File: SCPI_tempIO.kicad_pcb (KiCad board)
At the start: 2 copper layers, 40.4 x 21.5 mm, 27 parts, among them J1 Conn_ARM_JTAG_SWD_10, J2 Conn_02x05_Counter_Clockwise, J3 USB_C_Receptacle_USB2.0_14P, J4 Conn_01x04_Pin, J5 Conn_01x04_Pin, SW1 SW_SPST, U1 STM32G070KBTx, U2 AP2112K-3.3, U3 SHT4x

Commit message: more fancy
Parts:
- moved R21 4.21 mm to (89.2, 38.9)
- moved R20 3.45 mm to (89.2, 40.7)
- moved R19 2.68 mm to (89.2, 42.5)
- moved R18 1.92 mm to (89.2, 44.3)
- moved R15 1.42 mm to (87.3, 49.1)
- moved R14 1.41 mm to (87.3, 50.2)
- moved R17 1.19 mm to (89.2, 46.1)
- moved R16 0.58 mm to (89.2, 48.0)
- moved J2 0.30 mm to (98.6, 52.7)
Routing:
- net /3v3: track 28.2 -> 47.0 mm
- net Net-(J2-Pin_3): track 0.00 -> 12.2 mm
- net Net-(J2-Pin_7): track 0.39 -> 11.2 mm
- net Net-(J2-Pin_5): track 0.00 -> 10.5 mm
- net Net-(J2-Pin_9): track 0.00 -> 10.4 mm
- net Net-(J2-Pin_2): track 0.00 -> 9.28 mm
- net Net-(J2-Pin_8): track 0.00 -> 8.57 mm
- net Net-(J2-Pin_6): track 0.00 -> 7.72 mm
- net Net-(J2-Pin_4): track 0.00 -> 7.27 mm
- net Net-(U1-PA7): track 1.92 -> 7.79 mm
- net Net-(U1-PA6): track 1.82 -> 5.62 mm
- net Net-(U1-PA5): track 1.71 -> 4.34 mm
- net Net-(U1-PA4): track 1.61 -> 3.46 mm
- net Net-(U1-PA0): track 4.66 -> 3.23 mm
- net Net-(U1-PA1): track 2.93 -> 1.52 mm
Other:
- board size 40.4 x 21.5 mm -> 40.3 x 21.4 mm

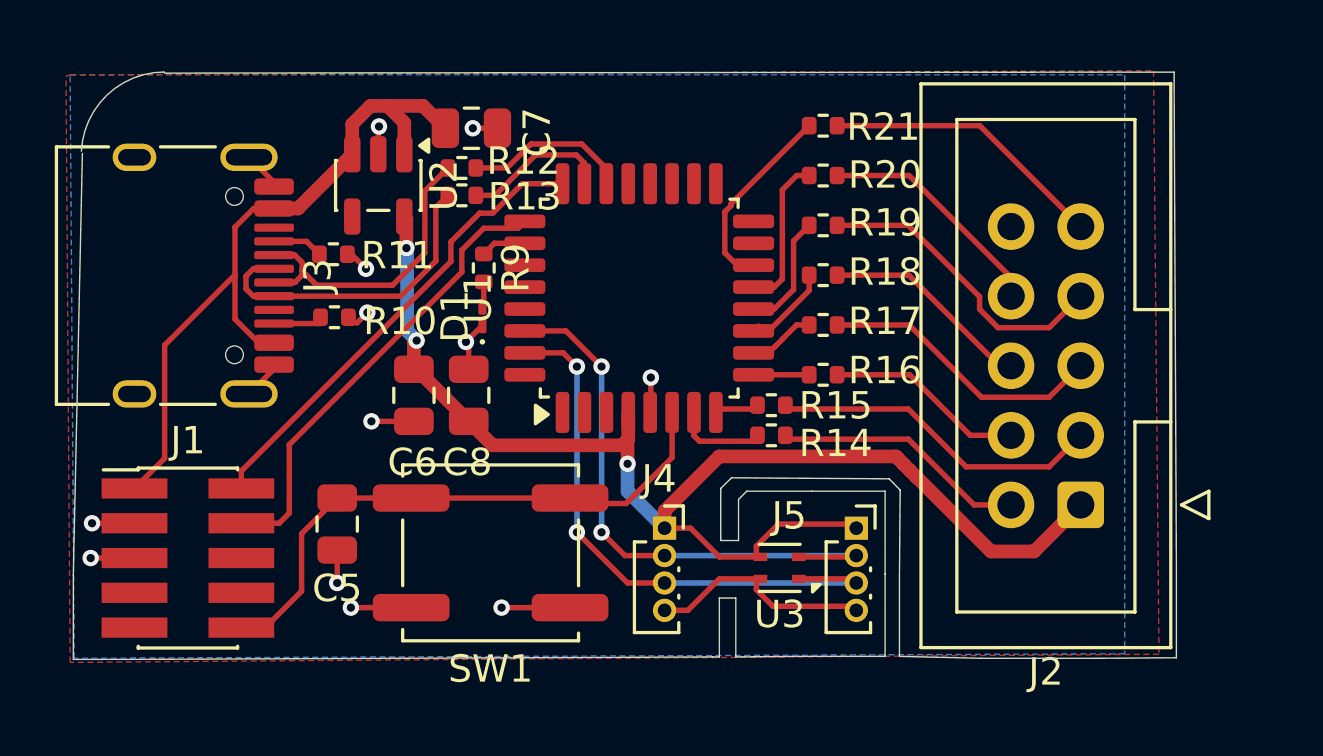
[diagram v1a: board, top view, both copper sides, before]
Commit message: pullups and cap for the SHT4x
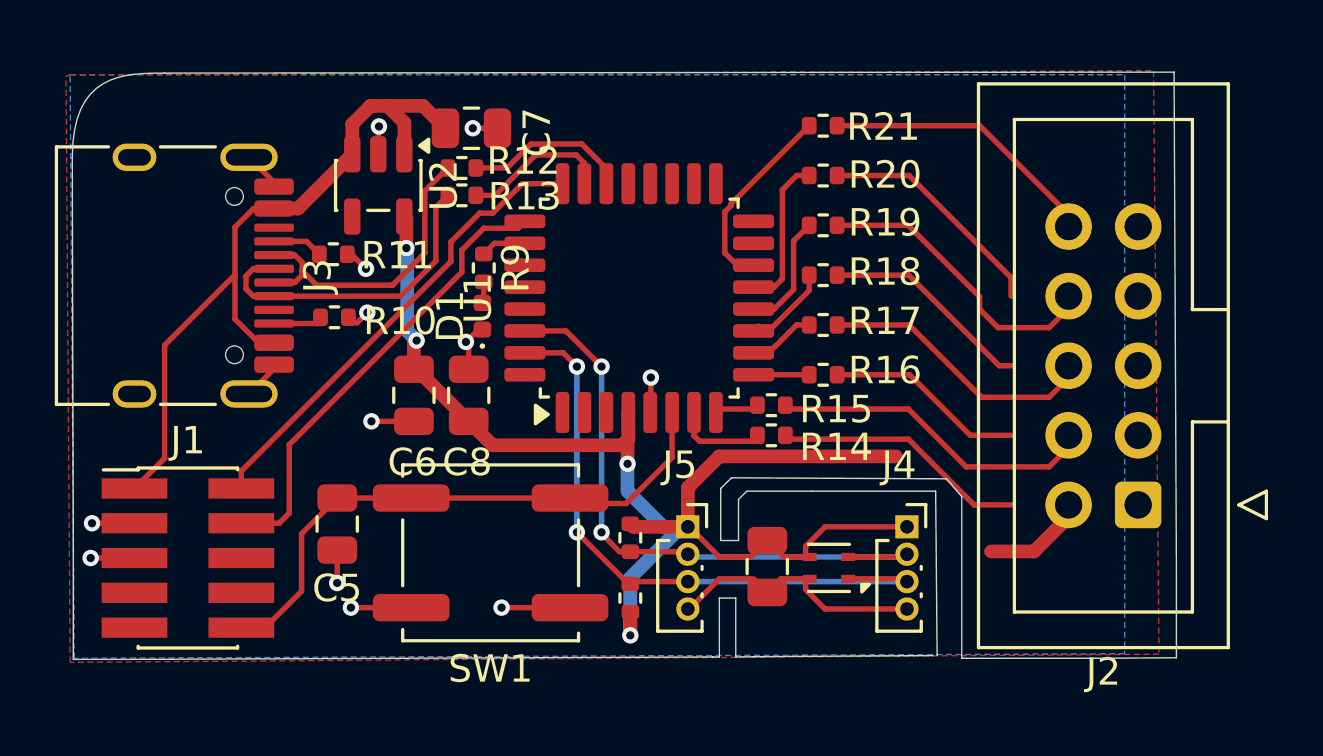
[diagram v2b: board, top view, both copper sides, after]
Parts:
- added C9: 100n, Capacitor_SMD:C_0805_2012Metric, F.Cu at (87.2, 55.0)
- added R23: 10k, Resistor_SMD:R_0402_1005Metric, F.Cu at (82.2, 53.9)
- added R24: 10k, Resistor_SMD:R_0402_1005Metric, F.Cu at (82.2, 56.1)
- D1: footprint LED_SMD:LED_01005_0402Metric_Pad0.57x0.30mm_HandSolder -> LED_SMD:LED_0402_1005Metric
- moved J4 8.85 mm to (92.3, 53.5)
- moved J5 6.15 mm to (84.3, 53.5)
- moved J2 2.10 mm to (100.7, 52.7)
- moved U3 1.80 mm to (89.5, 55.0)
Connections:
- net Net-(J4-Pin_2) renamed /SHT4x_sub/SCL
- net Net-(J4-Pin_3) renamed /SHT4x_sub/SDA
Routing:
- net Net-(J2-Pin_2): track 9.28 -> 13.3 mm
- net /SHT4x_sub/SDA: track 21.2 -> 23.3 mm
- net /SHT4x_sub/SCL: track 21.2 -> 23.2 mm
- net GND: track 28.7 -> 30.4 mm
- net /3v3: track 47.0 -> 47.8 mm, vias 3 -> 4
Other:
- outline, holes or cut-outs redrawn

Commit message: sent to JLC noodleUSBp16
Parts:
- added G***: LOGO, LOGO, B.Cu at (89.9, 45.9)
- moved R16 0.77 mm to (90.0, 47.9)
- moved R17 0.77 mm to (90.0, 46.1)
- moved R18 0.77 mm to (90.0, 44.3)
- moved R19 0.77 mm to (90.0, 42.5)
- moved R20 0.77 mm to (90.0, 40.6)
- moved R21 0.77 mm to (90.0, 38.8)
- moved R24 0.31 mm to (82.2, 55.8)
- moved J4 0.25 mm to (92.5, 53.6)
- moved C9 0.25 mm to (87.5, 55.0)
- moved D1 0.21 mm to (76.8, 46.0)
- moved C7 0.20 mm to (76.4, 38.8)
- moved R12 0.20 mm to (75.8, 40.4)
- moved R13 0.20 mm to (75.8, 41.4)
- moved U3 0.20 mm to (89.7, 55.0)
- moved J1 0.16 mm to (66.2, 54.6)
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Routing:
- net /3v3: track 47.8 -> 58.4 mm
- net Net-(J2-Pin_3): track 12.2 -> 14.3 mm
- net Net-(J2-Pin_7): track 11.2 -> 13.1 mm
- net Net-(J2-Pin_2): track 13.3 -> 11.4 mm
- net Net-(J2-Pin_8): track 8.57 -> 10.3 mm
- net GND: track 30.4 -> 28.7 mm, vias 12 -> 24
- net Net-(J2-Pin_4): track 7.27 -> 8.61 mm
- net Net-(J2-Pin_6): track 7.72 -> 9.07 mm
- net Net-(J2-Pin_5): track 10.5 -> 11.8 mm
- net Net-(J2-Pin_9): track 10.4 -> 11.8 mm
- net Net-(U1-PA2): track 2.03 -> 2.82 mm
- net Net-(U1-PA3): track 2.55 -> 3.33 mm
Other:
- board size 40.3 x 21.4 mm -> 42.6 x 22.2 mm
- board text added: "SCPI-TEMPIO"
- board text added: "for all your temperature, humidity and other IO needs. Break off the SHT40 part and connect it using a 4 lead wire for more flexibility."
- board text added: "nacho.works"
- board text added: "▼▲▼"
